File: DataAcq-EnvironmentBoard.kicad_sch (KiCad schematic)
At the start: 29 parts, among them J1 Airflow Breakout, J2 CAN Output, J3 CAN Input, J4 Humidity Breakout, J5 Temp Breakout, U4 Daughterboard Connector

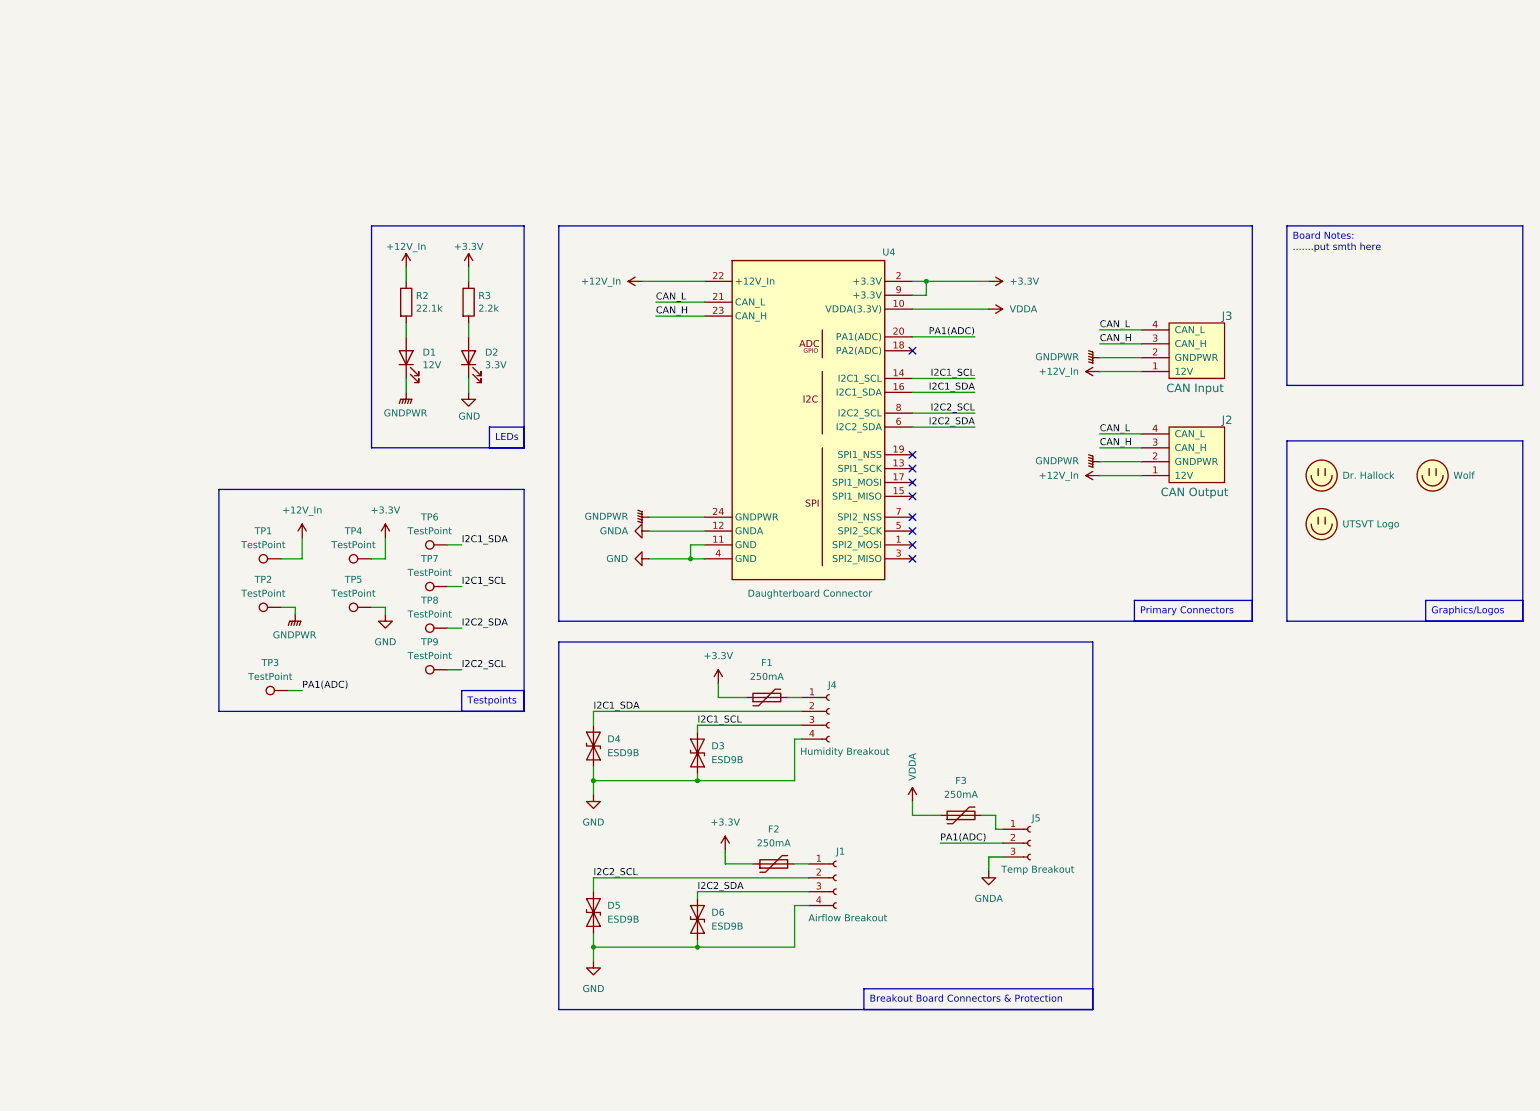
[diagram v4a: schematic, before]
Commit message: change sch for one connector design
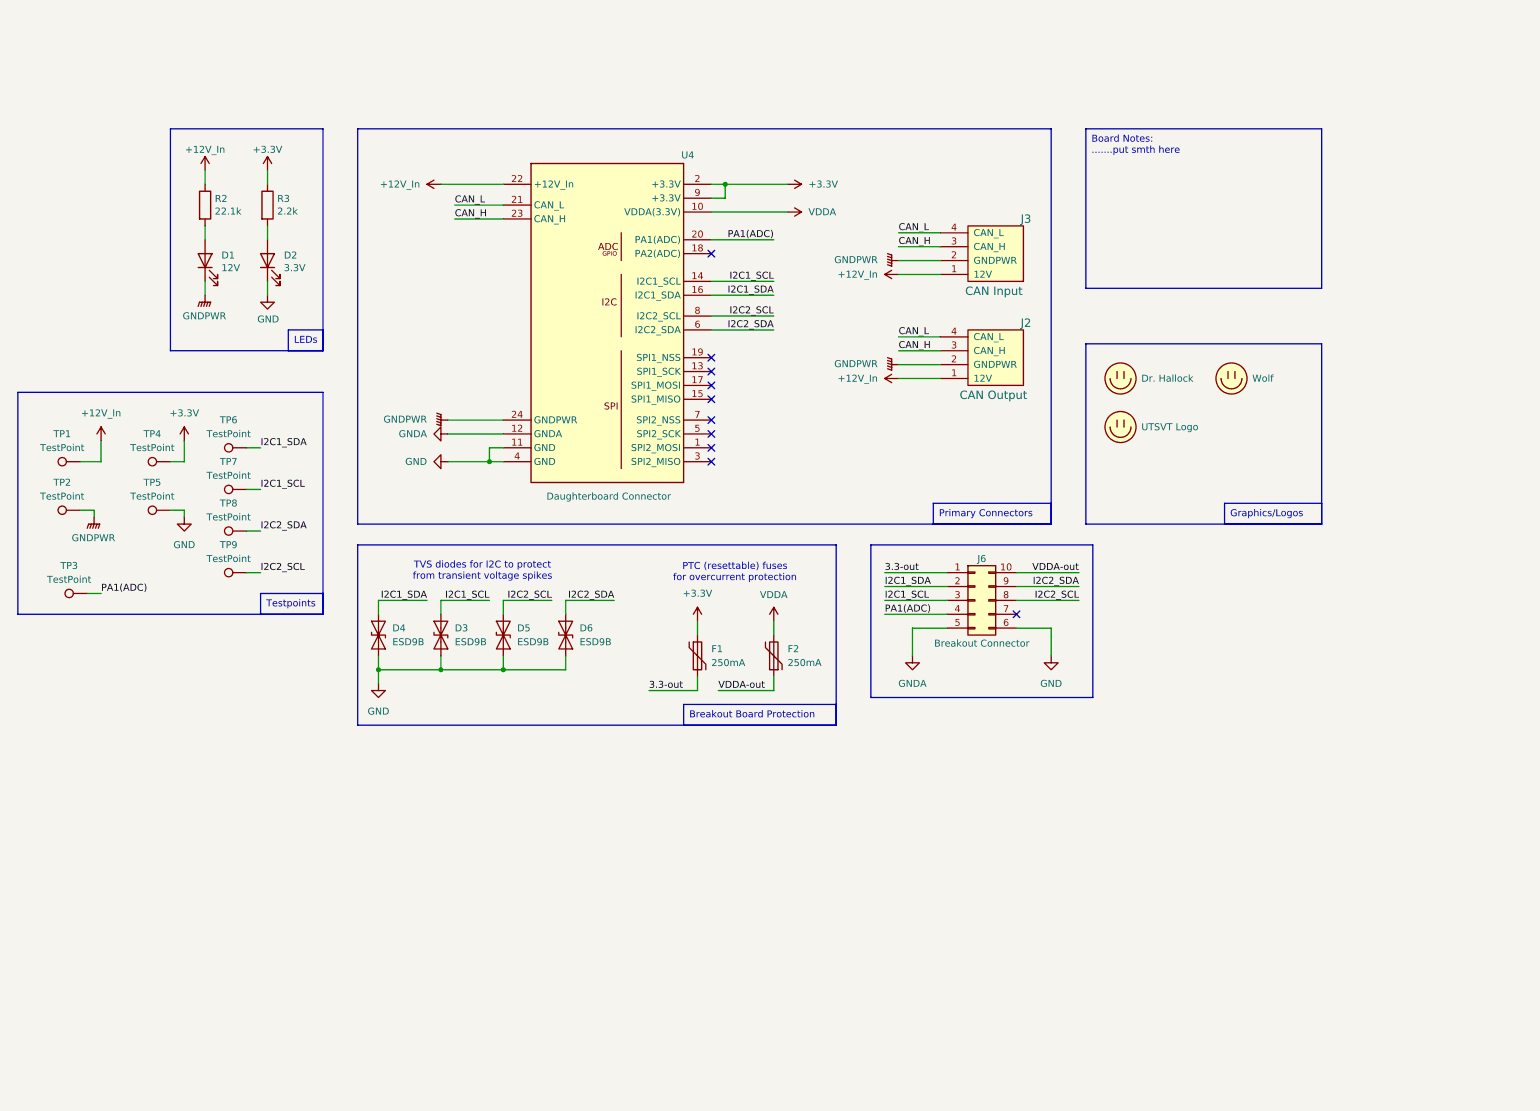
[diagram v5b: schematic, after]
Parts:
- removed F3: 250mA, Fuse:Fuse_0603_1608Metric, symbol Device:Polyfuse
- removed J1: Airflow Breakout, UTSVT_Connectors:Molex_MicroFit3.0_1x4xP3.00mm_PolarizingPeg_Vertical, symbol Connector:Conn_01x04_Socket
- removed J4: Humidity Breakout, UTSVT_Connectors:Molex_MicroFit3.0_1x4xP3.00mm_PolarizingPeg_Vertical, symbol Connector:Conn_01x04_Socket
- removed J5: Temp Breakout, UTSVT_Connectors:Molex_MicroFit3.0_1x3xP3.00mm_PolarizingPeg_Vertical, symbol Connector:Conn_01x03_Socket
- added J6: Breakout Connector, Connector_Molex:Molex_Nano-Fit_105310-xx10_2x05_P2.50mm_Vertical, symbol Connector_Generic:Conn_02x05_Counter_Clockwise
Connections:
- net +3.3V: no longer F2.1
- net GND: now also J6.6 (Pin_6)
- net GNDA: now also J6.5 (Pin_5)
- net I2C1_SCL: now also J6.3 (Pin_3)
- net I2C1_SDA: now also J6.2 (Pin_2)
- net I2C2_SCL: now also J6.8 (Pin_8)
- net I2C2_SDA: now also J6.9 (Pin_9)
- net PA1(ADC): now also J6.4 (Pin_4)
- net VDDA: now also F2.2
- net 3.3-out: now reaches F1.2
- net 3.3-out: now also J6.1 (Pin_1)
- new net VDDA-out: F2.1, J6.10 (Pin_10)
- no-connect marks 9 -> 10
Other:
- note added: "PTC (resettable) fuses for overcurrent protection"
- note added: "TVS diodes for I2C to protect from transient voltage spikes"
- moved on the sheet: D1, D2, D3, D4, D5, D6, F1, J2, J3, R2, R3, TP1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

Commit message: sch: add sensors back for testing
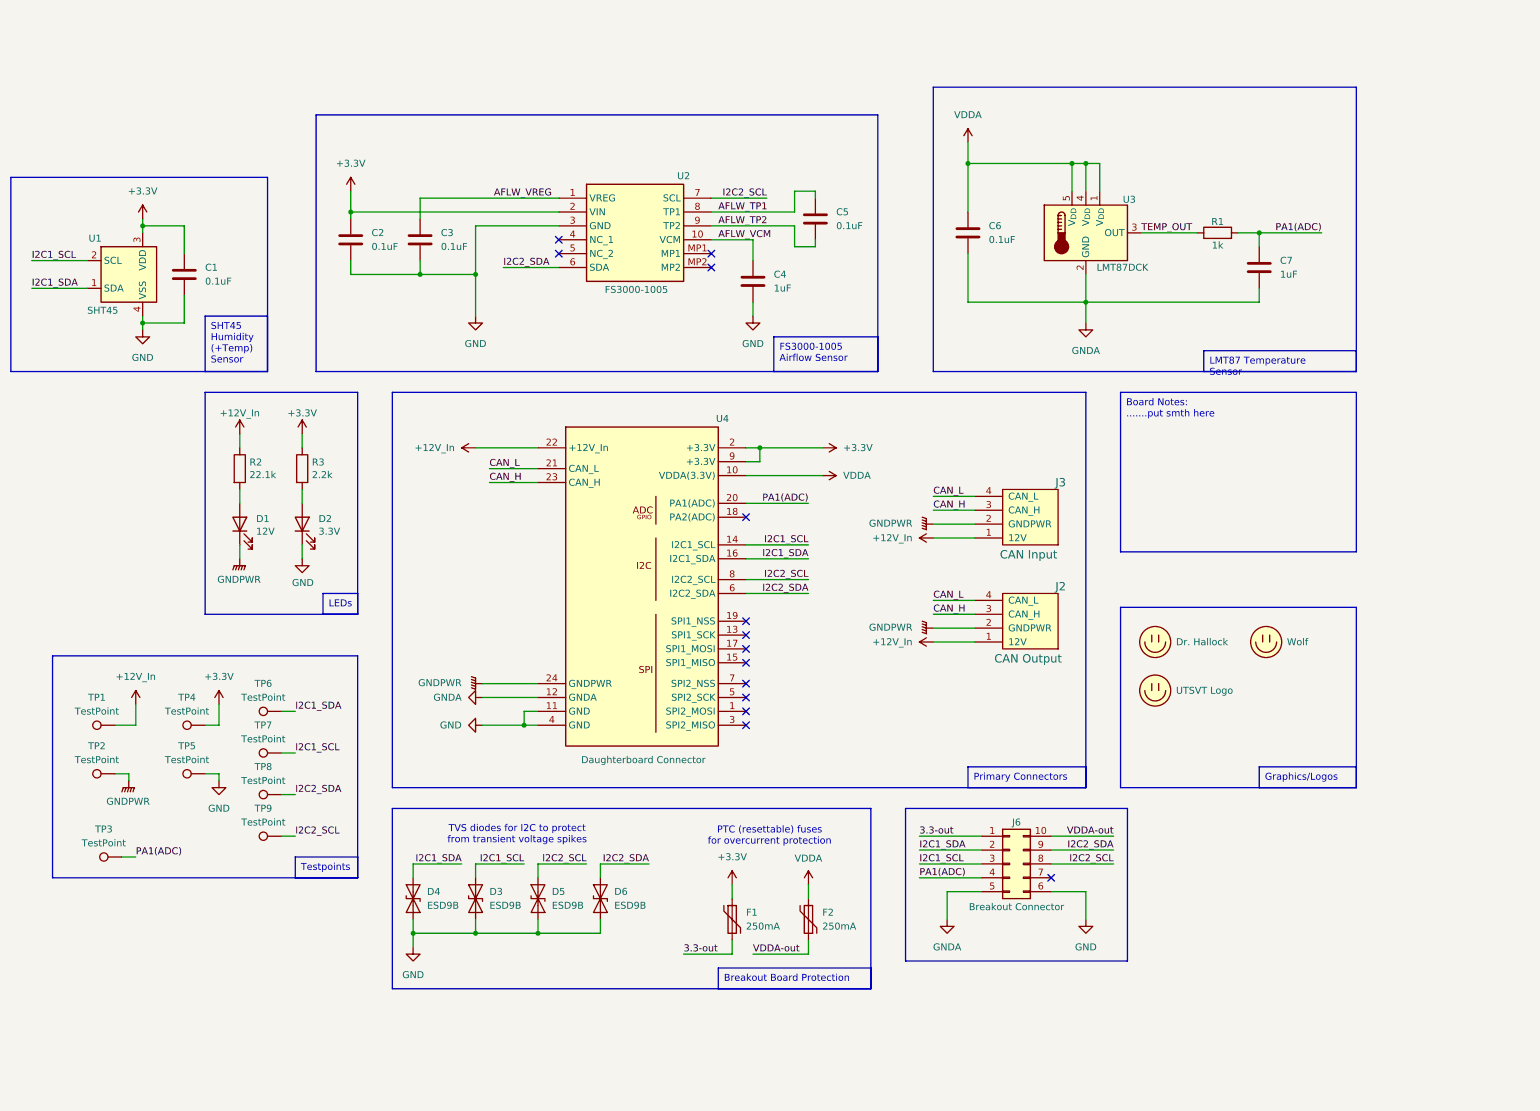
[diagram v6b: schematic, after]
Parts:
- added C1, C2, C3, C5, C6: 0.1uF, Capacitor_SMD:C_0805_2012Metric, symbol Device:C
- added C4, C7: 1uF, Capacitor_SMD:C_0805_2012Metric, symbol Device:C
- added R1: 1k, Resistor_SMD:R_0805_2012Metric, symbol Device:R
- added U1: SHT45, Sensor_Humidity:Sensirion_DFN-4_1.5x1.5mm_P0.8mm_SHT4x_NoCentralPad, symbol Sensor_Humidity:SHT4x
- added U2: FS3000-1005, SamacSys_Parts:FS30001005, symbol SamacSys_Parts:FS3000-1005
- added U3: LMT87DCK, Package_TO_SOT_SMD:SOT-353_SC-70-5, symbol Sensor_Temperature:LMT87DCK
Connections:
- net +3.3V: now also C1.1, C2.1, U1.3 (VDD), U2.2 (VIN)
- net GND: now also C1.2, C2.2, C3.2, C4.2, U1.4 (VSS), U2.3 (GND)
- net GNDA: now also C6.2, C7.2, U3.2 (GND)
- net I2C1_SCL: now also U1.2 (SCL)
- net I2C1_SDA: now also U1.1 (SDA)
- net I2C2_SCL: now also U2.7 (SCL)
- net I2C2_SDA: now also U2.6 (SDA)
- net PA1(ADC): now also C7.1, R1.2
- net VDDA: now also C6.1, U3.1 (V_{DD}), U3.4 (V_{DD}), U3.5 (V_{DD})
- new net AFLW_TP1: C5.1, U2.8 (TP1)
- new net AFLW_TP2: C5.2, U2.9 (TP2)
- new net AFLW_VCM: C4.1, U2.10 (VCM)
- new net AFLW_VREG: C3.1, U2.1 (VREG)
- new net TEMP_OUT: R1.1, U3.3 (OUT)
- no-connect marks 10 -> 14
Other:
- moved on the sheet: D1, D2, D3, D4, D5, D6, F1, F2, J2, J3, J6, R2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

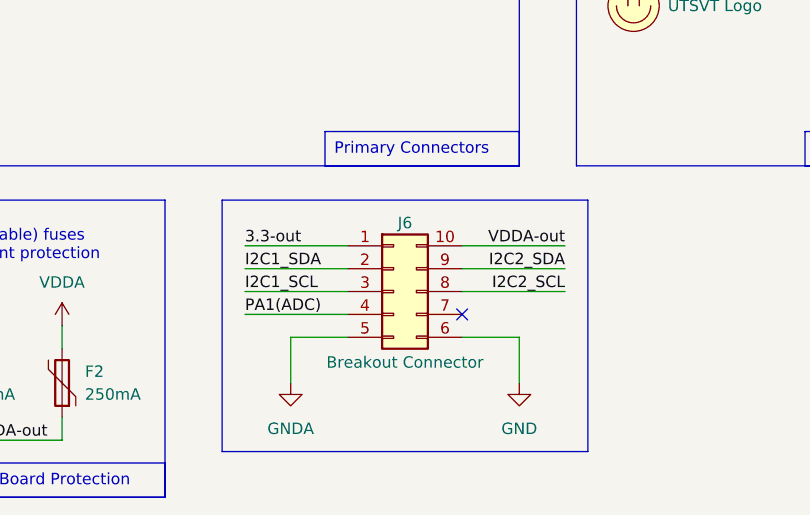
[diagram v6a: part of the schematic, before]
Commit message: rearrange connector to match breakout
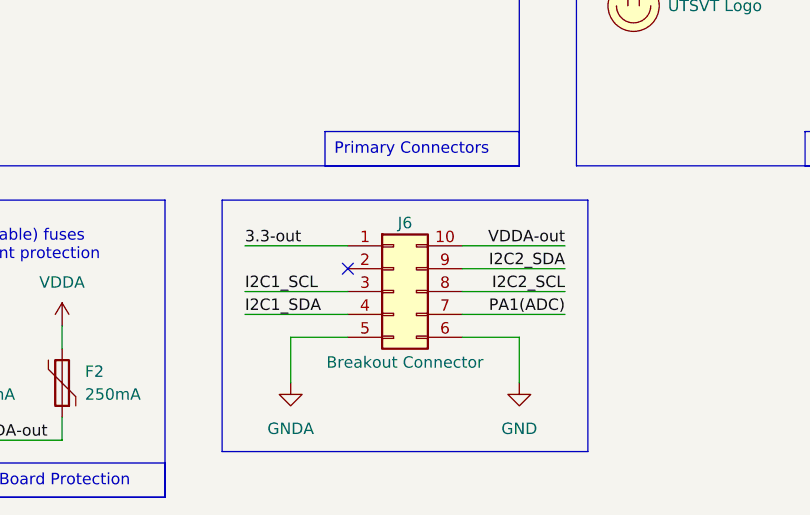
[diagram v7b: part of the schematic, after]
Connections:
- net I2C1_SDA: now also J6.4 (Pin_4); no longer J6.2 (Pin_2)
- net PA1(ADC): now also J6.7 (Pin_7); no longer J6.4 (Pin_4)

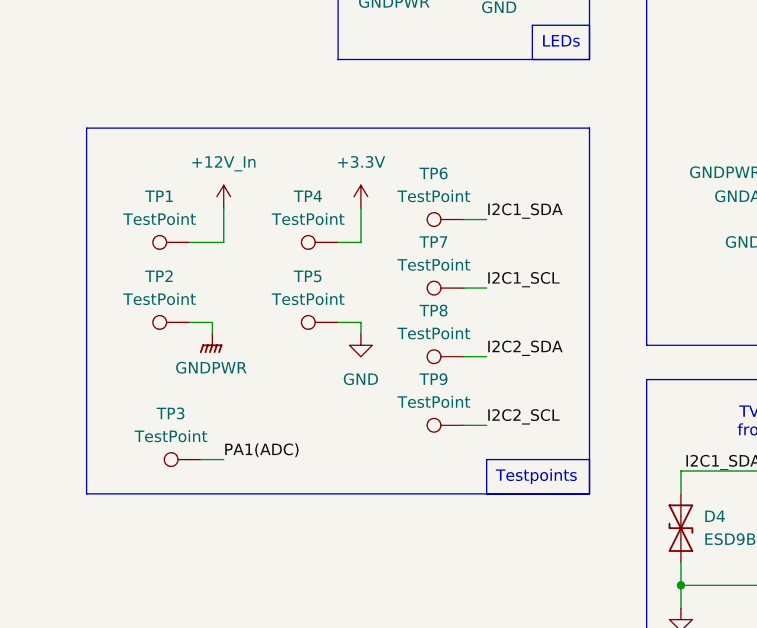
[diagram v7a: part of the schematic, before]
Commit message: traces for connector change
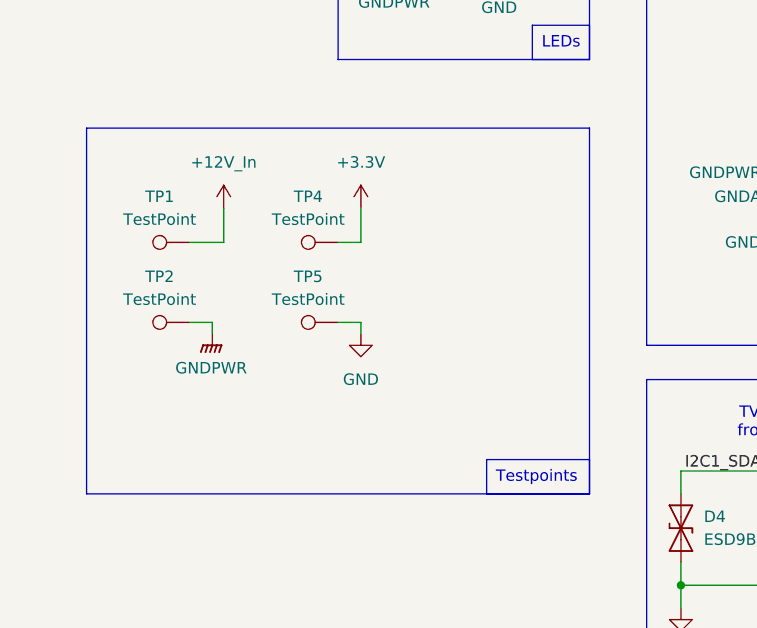
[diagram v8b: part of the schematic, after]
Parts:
- removed TP3, TP6, TP7, TP8, TP9: TestPoint, Connector_PinHeader_2.54mm:PinHeader_1x01_P2.54mm_Vertical, symbol Connector:TestPoint
